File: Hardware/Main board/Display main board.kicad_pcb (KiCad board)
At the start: 2 copper layers, 133.4 x 78.8 mm, 23 parts, among them J1 Conn_01x08_Socket

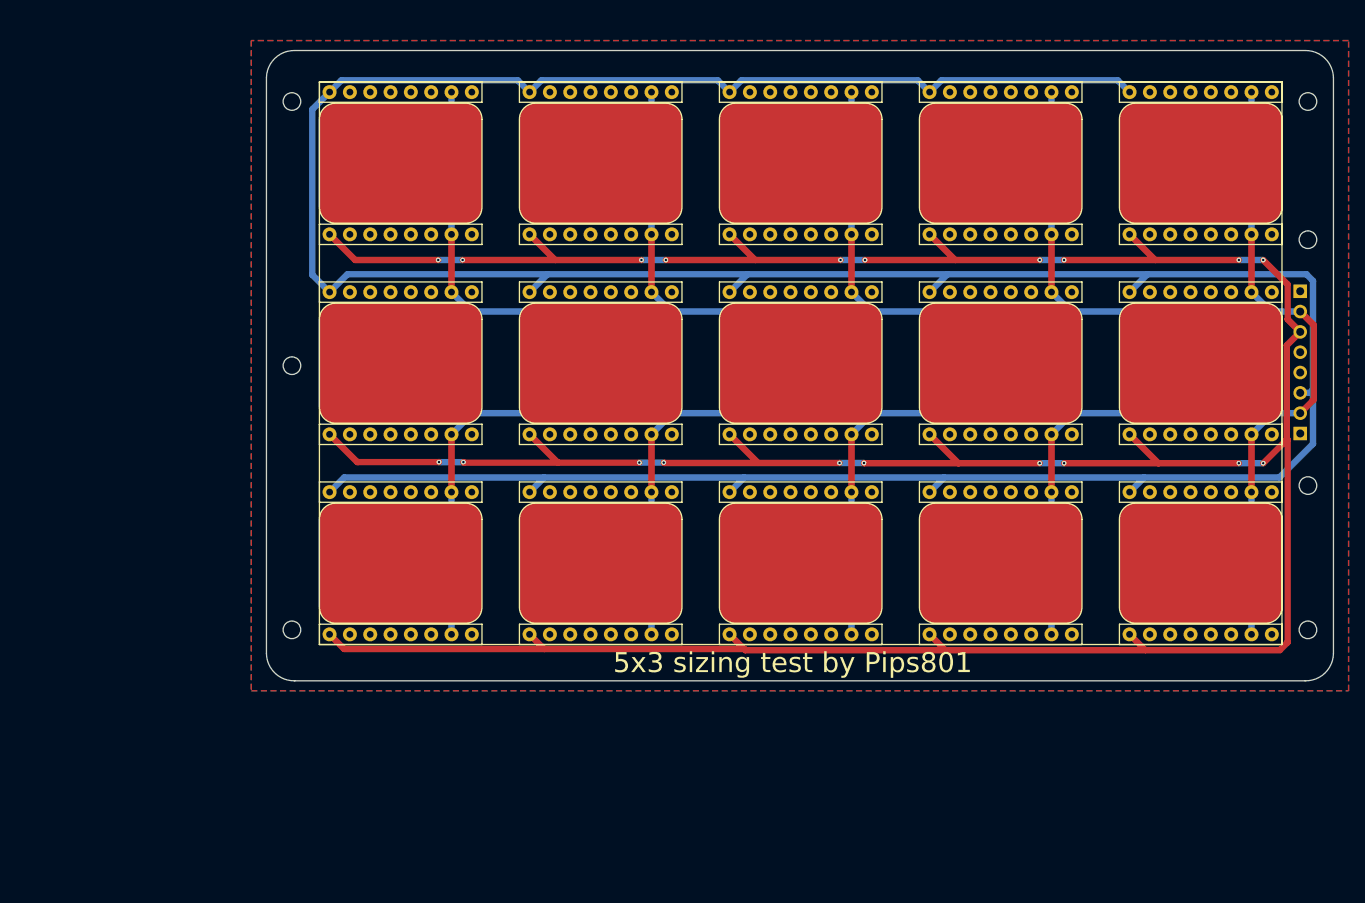
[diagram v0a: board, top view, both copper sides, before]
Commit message: Big changes
- Folder changes
- change dimensions of board to match thicker material
- begin part selection/footprint selection
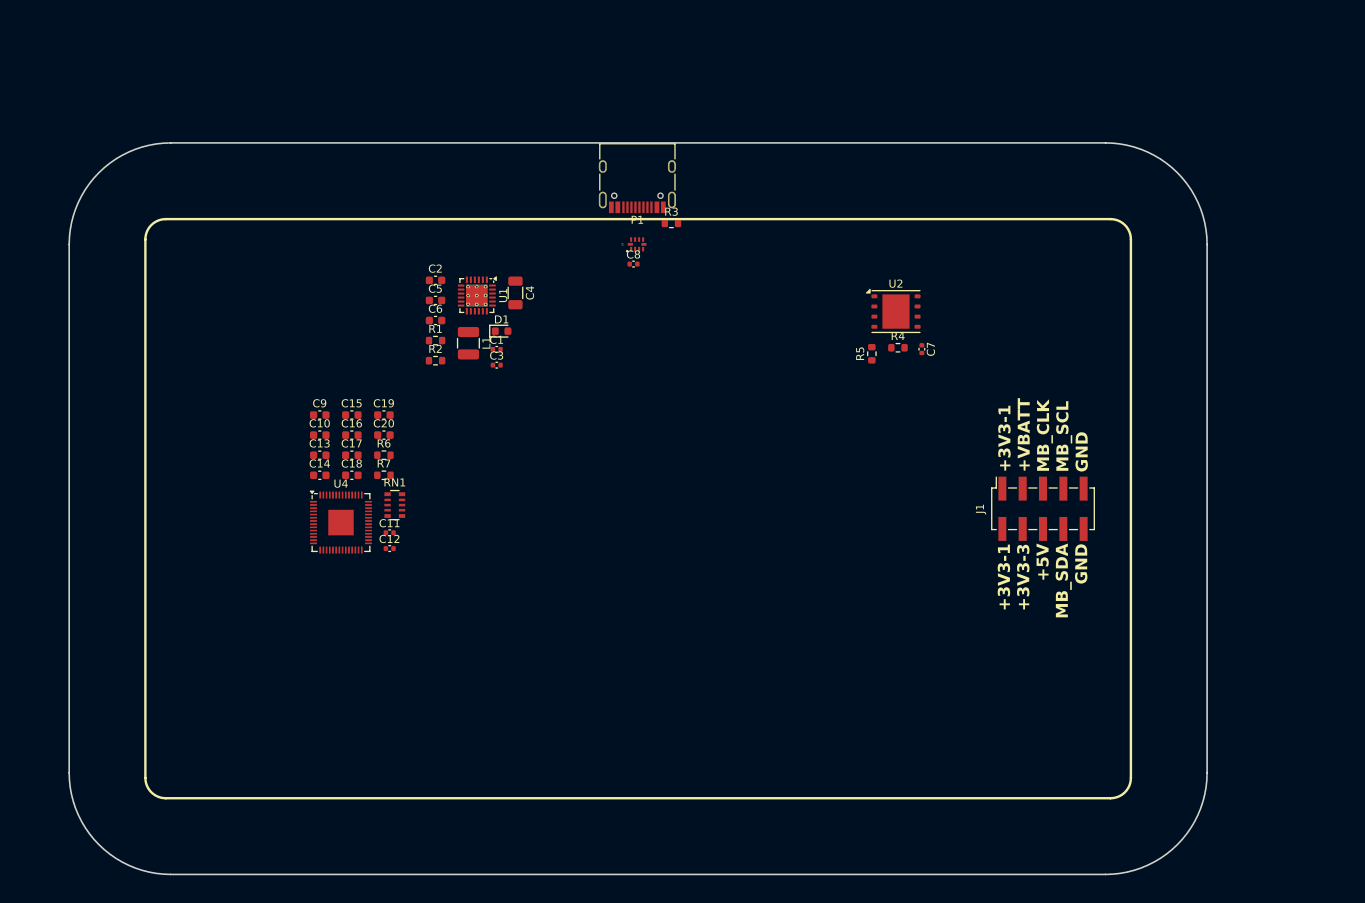
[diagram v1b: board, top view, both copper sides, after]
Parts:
- removed MB1, MB10, MB11, MB12, MB13, MB14, MB15, MB2, MB3, MB4, MB5, MB6, MB7, MB8, MB9: MiniBadge_Full, MiniBadge:MiniBadge_Slot_Reflective
- removed REF** (x7): MountingHole_2.2mm_M2, MountingHole:MountingHole_2.2mm_M2
- added C1: 1µF, Capacitor_SMD:C_0402_1005Metric, F.Cu at (119.6, 76.7)
- added C10: 10µF, Capacitor_SMD:C_0603_1608Metric, F.Cu at (97.5, 87.4)
- added C11: 1µF, Capacitor_SMD:C_0402_1005Metric, F.Cu at (106.2, 99.6)
- added C12: 1µF, Capacitor_SMD:C_0402_1005Metric, F.Cu at (106.2, 101.6)
- added C13: 10µF, Capacitor_SMD:C_0603_1608Metric, F.Cu at (97.5, 89.9)
- added C14: 10µF, Capacitor_SMD:C_0603_1608Metric, F.Cu at (97.5, 92.4)
- added C15: 10µF, Capacitor_SMD:C_0603_1608Metric, F.Cu at (101.5, 84.9)
- added C16: 10µF, Capacitor_SMD:C_0603_1608Metric, F.Cu at (101.5, 87.4)
- added C17: 10µF, Capacitor_SMD:C_0603_1608Metric, F.Cu at (101.5, 89.9)
- added C18: 10µF, Capacitor_SMD:C_0603_1608Metric, F.Cu at (101.5, 92.4)
- added C19: 10µF, Capacitor_SMD:C_0603_1608Metric, F.Cu at (105.5, 84.9)
- added C2: 10µF, Capacitor_SMD:C_0603_1608Metric, F.Cu at (111.9, 68.1)
- added C20: 10µF, Capacitor_SMD:C_0603_1608Metric, F.Cu at (105.5, 87.4)
- added C3: 47nF, Capacitor_SMD:C_0402_1005Metric, F.Cu at (119.6, 78.7)
- added C4: 60μF, Capacitor_SMD:C_1206_3216Metric, F.Cu at (121.9, 69.6)
- added C5: 10µF, Capacitor_SMD:C_0603_1608Metric, F.Cu at (111.9, 70.6)
- added C6: 10µF, Capacitor_SMD:C_0603_1608Metric, F.Cu at (111.9, 73.1)
- added C7: 0.1μF, Capacitor_SMD:C_0402_1005Metric, F.Cu at (172.7, 76.7)
- added C8: 0.1μF, Capacitor_SMD:C_0402_1005Metric, F.Cu at (136.7, 66.0)
- added C9: 10µF, Capacitor_SMD:C_0603_1608Metric, F.Cu at (97.5, 84.9)
- added D1: 20v 5A, Diode_SMD:D_0603_1608Metric, F.Cu at (120.2, 74.4)
- added L1: 2.2µH, Inductor_SMD:L_1210_3225Metric, F.Cu at (116.0, 75.9)
- added P1: USB_C_Plug_USB2.0, Connector_USB:USB_C_Receptacle_HRO_TYPE-C-31-M-12, F.Cu at (137.2, 54.9)
- added R1: R_Small, Resistor_SMD:R_0603_1608Metric, F.Cu at (111.9, 75.6)
- added R2: R_Small, Resistor_SMD:R_0603_1608Metric, F.Cu at (111.9, 78.1)
- added R3: 5.1k, Resistor_SMD:R_0603_1608Metric, F.Cu at (141.4, 61.0)
- added R4: 5.1k, Resistor_SMD:R_0603_1608Metric, F.Cu at (169.7, 76.5)
- added R5: 1kΩ, Resistor_SMD:R_0603_1608Metric, F.Cu at (166.5, 77.2)
- added R6: 27.4Ω, Resistor_SMD:R_0603_1608Metric, F.Cu at (105.5, 89.9)
- added R7: 27.4Ω, Resistor_SMD:R_0603_1608Metric, F.Cu at (105.5, 92.4)
- added RN1: R_Pack05, Resistor_SMD:R_Array_Convex_5x0603, F.Cu at (106.8, 96.2)
- added U1: BQ25895RTW, Package_DFN_QFN:Texas_RTW_WQFN-24-1EP_4x4mm_P0.5mm_EP2.7x2.7mm_ThermalVias, F.Cu at (117.1, 70.0)
- added U2: W25Q32JVSS, Package_SON:WSON-8-1EP_6x5mm_P1.27mm_EP3.4x4.3mm, F.Cu at (169.5, 72.0)
- added U3: ~, TS3USB221A:QFN-10-RSE, F.Cu at (137.1, 63.6)
- added U4: RP2040, Package_DFN_QFN:QFN-56-1EP_7x7mm_P0.4mm_EP3.2x3.2mm, F.Cu at (100.1, 98.3)
- J1: value Conn_01x08_Socket -> Board to Board; footprint Connector_PinHeader_2.54mm:PinHeader_1x08_P2.54mm_Horizontal -> Connector_PinSocket_2.54mm:PinSocket_2x05_P2.54mm_Vertical_SMD; moved to F.Cu
- moved J1 33.5 mm to (187.9, 96.6), turned to 90 degrees
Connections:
- J1 pad 1: GND -> +3v3-1
- J1 pad 2: +3.3V -> +3v3-2
- J1 pad 3: +5V -> +3v3-3
- J1 pad 4: unconnected-(J1-Pin_4-Pad4) -> +VBATT
- J1 pad 5: unconnected-(J1-Pin_5-Pad5) -> +5V
- J1 pad 6: unconnected-(J1-Pin_6-Pad6) -> MB_CLK
- J1 pad 7: +3.3V -> MB_SDA
- J1 pad 8: GND -> MB_SCL
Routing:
- net +3.3V: track 507.1 -> 0.00 mm
- net CLK: track 461.3 -> 0.00 mm, vias 20 -> 0
- net +5V: track 426.4 -> 0.00 mm
- removed copper zone on B.Cu, net GND
- removed copper zone on F.Cu, net GND
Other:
- board size 133.4 x 78.8 mm -> 142.2 x 91.4 mm
- board text added: "+3V3-1 +3V3-3 +5V MB_SDA GND"
- board text added: "+3V3-1 +VBATT MB_CLK MB_SCL GND"
- board text removed: "${TITLE} by Pips801"
- board text removed: "GND 3V3 NC NC NC 5V 3V3 GND"
- board text removed: "PROTOTYPE"

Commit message: small chages
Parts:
- moved C7 79.1 mm to (93.9, 83.6), turned to 90 degrees
- moved U2 74.2 mm to (97.1, 88.3), turned to 180 degrees
- moved R4 73.2 mm to (96.9, 83.8), turned to 180 degrees
- moved R5 66.6 mm to (100.1, 83.0), turned to -90 degrees
- moved C12 35.6 mm to (99.0, 66.8), turned to 90 degrees
- moved C11 34.1 mm to (97.0, 66.8), turned to 90 degrees
- moved RN1 32.9 mm to (93.5, 66.1), turned to 90 degrees
- moved R7 29.5 mm to (89.8, 67.5), turned to 90 degrees
- moved C19 29.0 mm to (82.3, 67.5), turned to 90 degrees
- moved R6 28.9 mm to (87.3, 67.5), turned to 90 degrees
- moved C20 28.7 mm to (84.8, 67.5), turned to 90 degrees
- moved U4 25.9 mm to (95.7, 72.9), turned to 180 degrees
- moved C18 24.0 mm to (89.8, 71.5), turned to 90 degrees
- moved C15 23.4 mm to (82.3, 71.5), turned to 90 degrees
- moved C17 23.2 mm to (87.3, 71.5), turned to 90 degrees
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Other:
- board text added: "+3V3-2 +VBATT MB_CLK MB_SCL GND"
- board text removed: "+3V3-1 +VBATT MB_CLK MB_SCL GND"

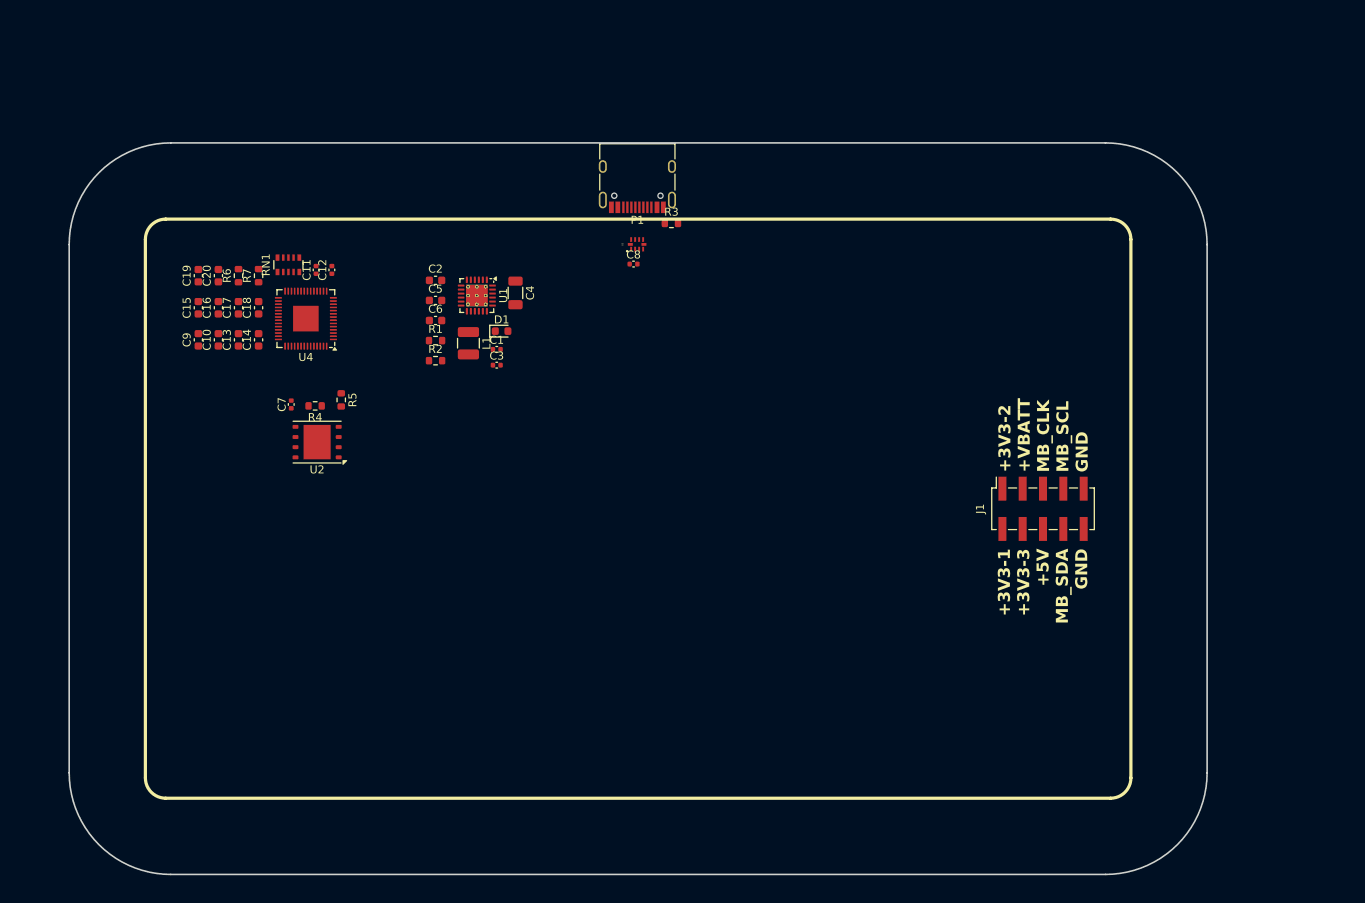
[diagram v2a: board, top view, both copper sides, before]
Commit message: hardware changes and initial traces/layout
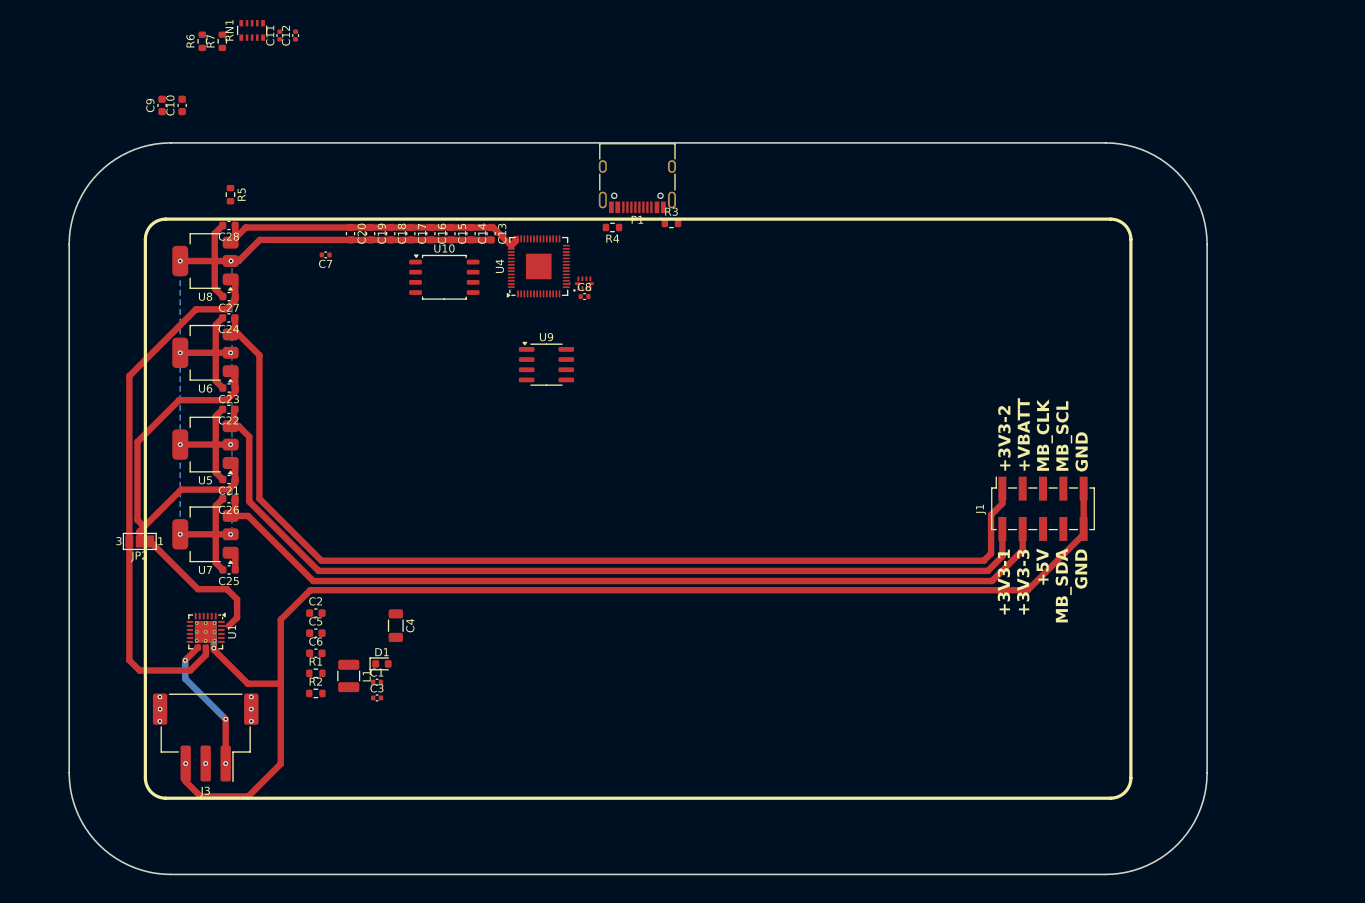
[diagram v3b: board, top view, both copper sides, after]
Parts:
- removed U2: W25Q32JVSS, Package_SON:WSON-8-1EP_6x5mm_P1.27mm_EP3.4x4.3mm
- added C21: 4.7μF, Capacitor_SMD:C_0603_1608Metric, F.Cu at (86.1, 93.0)
- added C22: 4.7μF, Capacitor_SMD:C_0603_1608Metric, F.Cu at (86.1, 84.2)
- added C23: 4.7μF, Capacitor_SMD:C_0603_1608Metric, F.Cu at (86.1, 81.5)
- added C24: 4.7μF, Capacitor_SMD:C_0603_1608Metric, F.Cu at (86.1, 72.8)
- added C25: 4.7μF, Capacitor_SMD:C_0603_1608Metric, F.Cu at (86.1, 104.3)
- added C26: 4.7μF, Capacitor_SMD:C_0603_1608Metric, F.Cu at (86.1, 95.4)
- added C27: 4.7μF, Capacitor_SMD:C_0603_1608Metric, F.Cu at (86.1, 70.1)
- added C28: 4.7μF, Capacitor_SMD:C_0603_1608Metric, F.Cu at (86.1, 61.2)
- added J3: Conn_01x03, Connector_JST:JST_XH_S3B-XH-SM4-TB_1x03-1MP_P2.50mm_Horizontal, F.Cu at (83.2, 125.2)
- added JP2: Voltage Select, Jumper:SolderJumper-3_P1.3mm_Bridged12_Pad1.0x1.5mm_NumberLabels, F.Cu at (75.0, 100.7)
- added U10: W25Q32JVSS, Package_SO:SOIC-8_5.23x5.23mm_P1.27mm, F.Cu at (113.0, 67.7)
- added U5: AP7361C-33E, Package_TO_SOT_SMD:SOT-223-3_TabPin2, F.Cu at (83.2, 88.6)
- added U6: AP7361C-33E, Package_TO_SOT_SMD:SOT-223-3_TabPin2, F.Cu at (83.2, 77.1)
- added U7: AP7361C-33E, Package_TO_SOT_SMD:SOT-223-3_TabPin2, F.Cu at (83.2, 99.8)
- added U8: AP7361C-33E, Package_TO_SOT_SMD:SOT-223-3_TabPin2, F.Cu at (83.2, 65.7)
- added U9: TPM8837C, Package_SO:SOIC-8_3.9x4.9mm_P1.27mm, F.Cu at (125.8, 78.6)
- R1: value R_Small -> 5.23k
- R2: value R_Small -> 30.1k
- RN1: value R_Pack05 -> 5x 10k
- moved U1 54.0 mm to (83.2, 112.0)
- moved C4 44.2 mm to (107.0, 111.2)
- moved C5 44.2 mm to (97.0, 112.2)
- moved R2 44.2 mm to (97.0, 119.7)
- moved C1 44.2 mm to (104.6, 118.3)
- moved C3 44.2 mm to (104.6, 120.3)
- moved D1 44.2 mm to (105.2, 116.0)
- moved C2 44.2 mm to (97.0, 109.7)
- moved C6 44.2 mm to (97.0, 114.7)
- moved L1 44.2 mm to (101.1, 117.5)
- moved R1 44.2 mm to (97.0, 117.2)
- moved R4 43.3 mm to (134.0, 61.5)
- moved C13 34.2 mm to (118.9, 62.2), turned to -90 degrees
- moved C15 32.9 mm to (113.9, 62.2), turned to -90 degrees
- moved U4 29.8 mm to (124.8, 66.3), turned to 90 degrees
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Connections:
- net Net-(BATT1-+) renamed /BMS/BATT+
- net Net-(U1-TS) renamed /BMS/NTC
- J1 pad 1: +3v3-1 -> +3v3-2
- J1 pad 2: +3v3-2 -> +3v3-1
- J1 pad 3: +3v3-3 -> +VBATT
- J1 pad 4: +VBATT -> +3v3-3
- J1 pad 5: +5V -> MB_CLK
- J1 pad 6: MB_CLK -> +5V
- J1 pad 7: MB_SDA -> MB_SCL
- J1 pad 8: MB_SCL -> MB_SDA
- U4 pad 12: unconnected-(U4-GPIO9-Pad12) -> /RP2040/IO9/MB_CLK
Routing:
- net GND: track 0.00 -> 255.1 mm, vias 0 -> 10
- net +3v3-2: track 0.00 -> 128.6 mm
- net +3v3-1: track 0.00 -> 115.2 mm
- net +3v3-3: track 0.00 -> 109.5 mm
- net +VBATT: track 0.00 -> 67.4 mm
- net /Power managment/VIN: track 0.00 -> 49.4 mm
- net +3.3V: track 0.00 -> 40.2 mm
- net +5V: track 0.00 -> 18.5 mm
- net /BMS/BATT+: track 0.00 -> 17.3 mm, vias 0 -> 3
- net /BMS/NTC: vias 0 -> 1
- net (no net): vias 0 -> 6
- added copper zone on B.Cu, net GND
